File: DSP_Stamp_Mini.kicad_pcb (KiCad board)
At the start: 2 copper layers, 50 x 50 mm, 67 parts, among them J1 Conn_01x10, J2 SM03B-SRSS-TB, J3 Conn_01x04, J4 USB_C_Receptacle_USB2.0_14P, J5 Conn_01x04, J6 Conn_01x10, J8 Conn_01x04, SW1 SW_Push, SW2 SW_Push, U1 RP2350_80QFN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

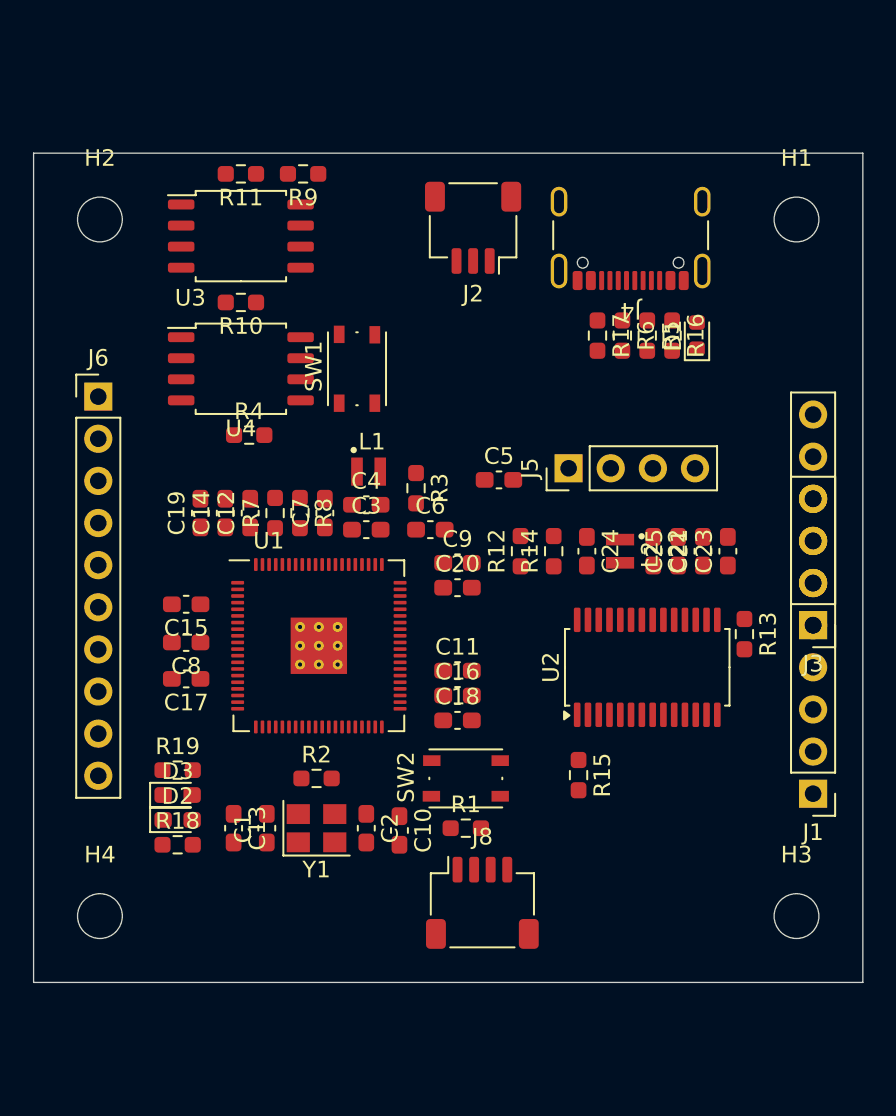
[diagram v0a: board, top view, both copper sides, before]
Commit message: switched pin headers to SMD, changed board shape and redid layout
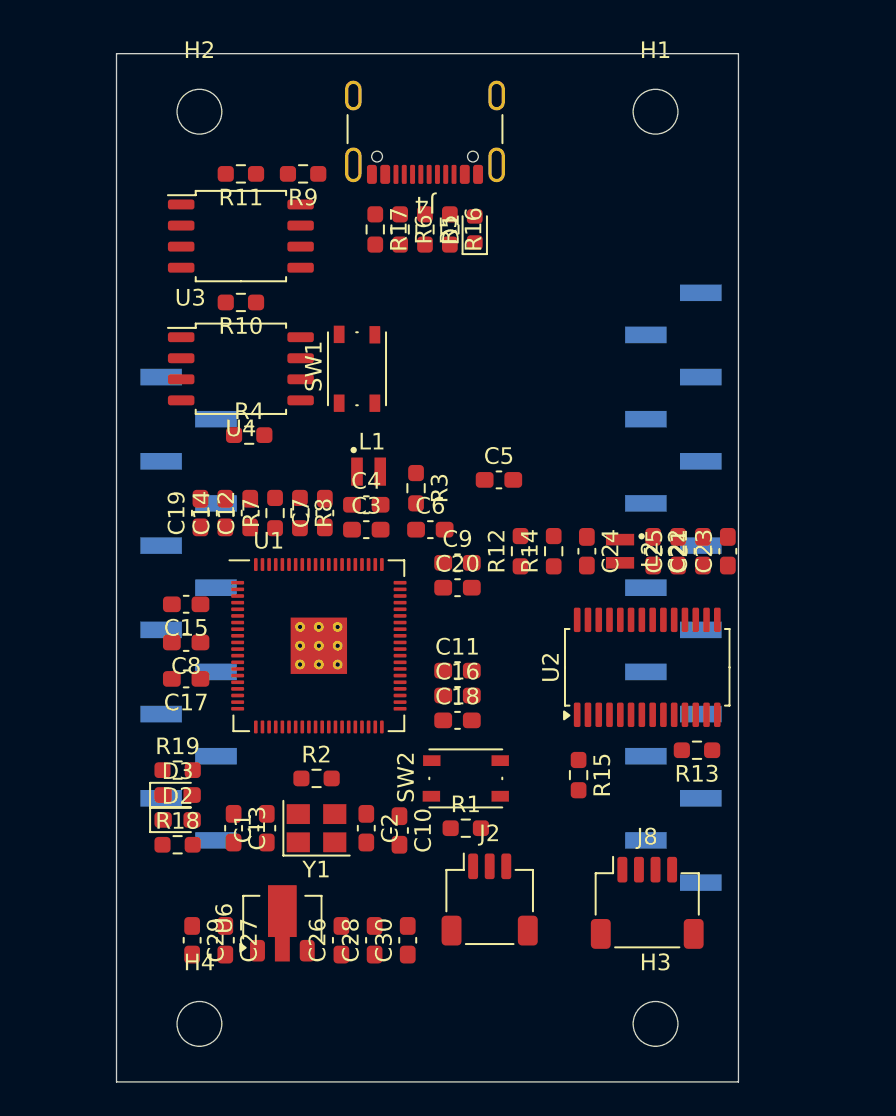
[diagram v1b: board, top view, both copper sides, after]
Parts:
- removed J5: Conn_01x04, Connector_PinHeader_2.54mm:PinHeader_1x04_P2.54mm_Vertical
- added C26: 100n, Capacitor_SMD:C_0603_1608Metric_Pad1.08x0.95mm_HandSolder, F.Cu at (103.6, 97.5)
- added C27: 100n, Capacitor_SMD:C_0603_1608Metric_Pad1.08x0.95mm_HandSolder, F.Cu at (96.6, 97.5)
- added C28: 100n, Capacitor_SMD:C_0603_1608Metric_Pad1.08x0.95mm_HandSolder, F.Cu at (105.6, 97.5)
- added C29: 10u, Capacitor_SMD:C_0603_1608Metric_Pad1.08x0.95mm_HandSolder, F.Cu at (94.6, 97.5)
- added C30: 10u, Capacitor_SMD:C_0603_1608Metric_Pad1.08x0.95mm_HandSolder, F.Cu at (107.6, 97.5)
- added J7: Conn_01x02, Connector_PinHeader_2.54mm:PinHeader_1x02_P2.54mm_Vertical_SMD_Pin1Right, B.Cu at (94.3, 64.8)
- added U6: AZ1117-3.3, Package_TO_SOT_SMD:SOT-89-3, F.Cu at (100.0, 96.1)
- J1, J6: footprint Connector_PinHeader_2.54mm:PinHeader_1x10_P2.54mm_Vertical -> Connector_PinHeader_2.54mm:PinHeader_1x10_P2.54mm_Vertical_SMD_Pin1Right; moved to B.Cu
- J3: value Conn_01x04 -> Conn_01x05; footprint Connector_PinHeader_2.54mm:PinHeader_1x04_P2.54mm_Vertical -> Connector_PinHeader_2.54mm:PinHeader_1x05_P2.54mm_Vertical_SMD_Pin1Right; moved to B.Cu
- moved J2 40.5 mm to (112.5, 95.0), turned to 0 degrees
- moved J3 17.2 mm to (123.6, 63.5), turned to 0 degrees
- moved J6 16.3 mm to (94.3, 80.0), turned to 180 degrees
- moved D1 14.8 mm to (111.6, 54.6)
- moved R16 14.8 mm to (110.1, 54.6)
- moved R17 14.8 mm to (105.6, 54.6)
- moved R5 14.8 mm to (108.6, 54.6)
- moved R6 14.8 mm to (107.1, 54.6)
- moved J4 14.0 mm to (108.6, 47.6)
- moved H1 10.7 mm to (122.5, 47.5)
- moved H3 10.7 mm to (122.5, 102.5)
- moved J1 10.4 mm to (123.6, 82.5), turned to 0 degrees
- moved J8 9.94 mm to (122.0, 95.2)
- moved H2 8.85 mm to (95.0, 47.5)
- moved H4 8.85 mm to (95.0, 102.5)
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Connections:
- J3 pad 2: GND -> /Vin_R
- J3 pad 3: /Vin_R -> GND
- J3 pad 4: GND -> /Vout_L
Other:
- board size 50 x 50 mm -> 37.5 x 62 mm
